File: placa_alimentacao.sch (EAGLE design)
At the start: 8 parts, among them IC1 7803TV

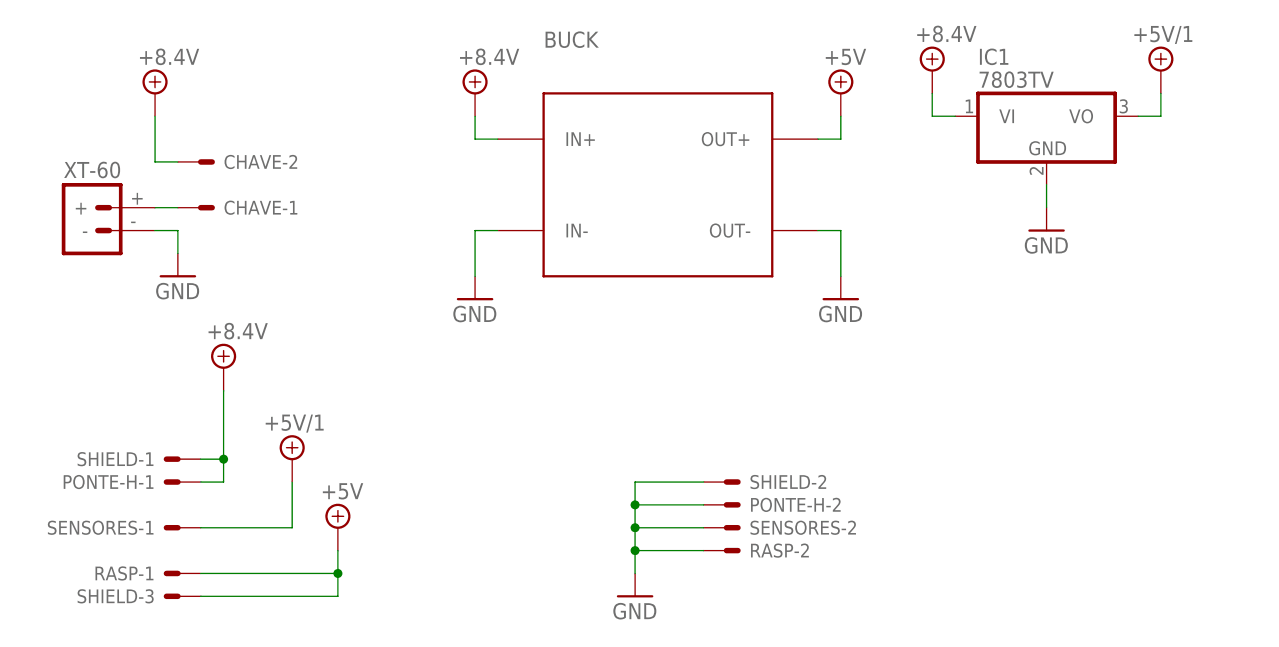
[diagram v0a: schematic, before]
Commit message: Adicionado regulador de tensão
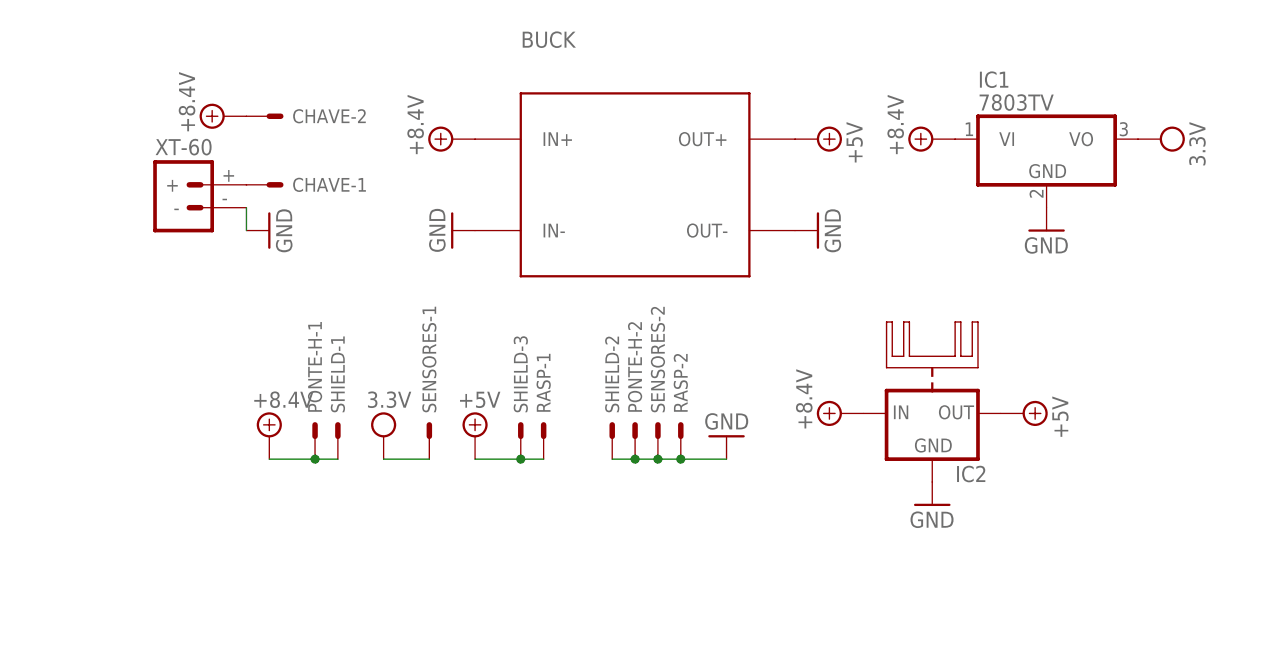
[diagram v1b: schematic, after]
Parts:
- added IC2: (no value), 78xx_with_heatsink:78XXH
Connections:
- net +5V/1 renamed VCC
- net +5V: now also IC2.OUT
- net +8V: now also IC2.IN
- net GND: now also IC2.GND
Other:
- moved on the sheet: BUCK, CHAVE-1, CHAVE-2, IC1, PONTE-H-1, PONTE-H-2, RASP-1, RASP-2, SENSORES-1, SENSORES-2, SHIELD-1, SHIELD-2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

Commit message: Erro tirado
Schematic and board insconsistentes
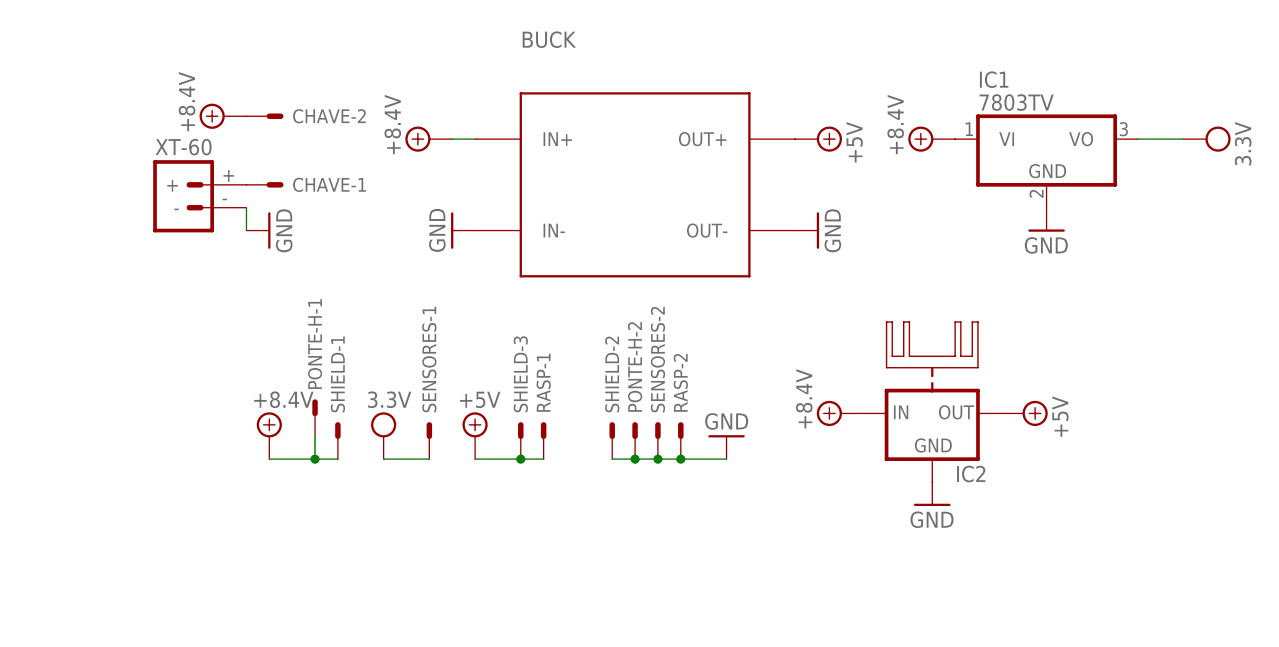
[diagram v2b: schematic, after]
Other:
- moved on the sheet: PONTE-H-1
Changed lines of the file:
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@@
 <instance part="GND3" gate="1" x="10.16" y="55.88" rot="R90"/>
 <instance part="SUPPLY1" gate="+8V" x="5.08" y="68.58" rot="R90"/>
-<instance part="SUPPLY2" gate="+8V" x="30.48" y="66.04" rot="R90"/>
+<instance part="SUPPLY2" gate="+8V" x="27.94" y="66.04" rot="R90"/>
 <instance part="SUPPLY3" gate="+5V" x="71.12" y="66.04" rot="R270"/>
-<instance part="PONTE-H" gate="-1" x="15.24" y="33.02" rot="R90"/>
 <instance part="PONTE-H" gate="-2" x="50.8" y="33.02" rot="R90"/>
 <instance part="SENSORES" gate="-1" x="27.94" y="33.02" rot="R90"/>
@@
 <instance part="SUPPLY10" gate="+5V" x="93.98" y="35.56" rot="R270"/>
 <instance part="SUPPLY5" gate="G$1" x="22.86" y="33.02"/>
-<instance part="3.3V" gate="G$1" x="109.22" y="66.04" rot="R270"/>
+<instance part="3.3V" gate="G$1" x="114.3" y="66.04" rot="R270"/>
+<instance part="PONTE-H" gate="-1" x="15.24" y="35.56" rot="R90"/>
 </instances>
 <busses>
@@
 <pinref part="BUCK" gate="G$1" pin="IN+"/>
 <pinref part="SUPPLY2" gate="+8V" pin="+8V"/>
+<wire x1="30.48" y1="66.04" x2="33.02" y2="66.04" width="0.1524" layer="91"/>
 </segment>
 <segment>
@@
 <segment>
 <pinref part="SUPPLY6" gate="+8V" pin="+8V"/>
-<pinref part="PONTE-H" gate="-1" pin="S"/>
 <wire x1="10.16" y1="30.48" x2="15.24" y2="30.48" width="0.1524" layer="91"/>
 <pinref part="SHIELD" gate="-1" pin="S"/>
 <wire x1="17.78" y1="30.48" x2="15.24" y2="30.48" width="0.1524" layer="91"/>
+<pinref part="PONTE-H" gate="-1" pin="S"/>
+<wire x1="15.24" y1="33.02" x2="15.24" y2="30.48" width="0.1524" layer="91"/>
 <junction x="15.24" y="30.48"/>
 </segment>
@@
 <pinref part="IC1" gate="A1" pin="VO"/>
 <pinref part="3.3V" gate="G$1" pin="VCC"/>
+<wire x1="111.76" y1="66.04" x2="106.68" y2="66.04" width="0.1524" layer="91"/>
 </segment>
 </net>
